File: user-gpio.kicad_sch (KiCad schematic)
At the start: 96 parts, among them J10 62732020621, J11 62703420621, J4 BM04B-SRSS-TB-LF-SN, J5 SSW-106-02-G-D-RA, J6 SSW-106-02-G-D-RA, J7 BM04B-SRSS-TB-LF-SN, J8 BM04B-SRSS-TB-LF-SN, J9 62704020621, Q10 BSS138PW, Q11 BSS138PW, Q12 IRLML6344TRPBF, Q13 BSS138PW, Q14 BSS138PW, Q15 BSS138PW, Q16 BSS138PW, Q8 BSS138PW, Q9 BSS138PW, SW2 CVS-08TB, U45 TPD4E05U06QDQARQ1, U46 TPD4E05U06QDQARQ1

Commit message: Updated schematic page fields
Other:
- company: (none) -> Antmicro Ltd.
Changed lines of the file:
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@@
   (title_block
     (title "K410T devboard")
-    (date "2023-01-04")
+    (date "2023-01-27")
     (rev "0.0.99")
+    (company "Antmicro Ltd.")
   )
   (junction (at 179.07 182.245) (diameter 0) (color 0 0 0 0)

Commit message: Adding JTAG to FMC connector - in progress
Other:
- company: Antmicro Ltd. -> (none)
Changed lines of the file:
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@@
   (title_block
     (title "K410T devboard")
-    (date "2023-01-27")
+    (date "2023-01-04")
     (rev "0.0.99")
-    (company "Antmicro Ltd.")
   )
   (junction (at 179.07 182.245) (diameter 0) (color 0 0 0 0)

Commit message: Updated local libraries
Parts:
- R168, R353, R354, R355, R356, R357, R358, R359, R360: footprint antmicro-footprints:0402-res -> K410T-devboard-footprints:0402-res; symbol antmicroResistors0402:R_100k_0402 -> K410T-devboard:R_100k_0402

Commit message: Bump revision to 1.0.0. Update name on schematic and PCB sheets
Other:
- title: K410T devboard -> Kintex 410T devboard

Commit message: Introduce component standardization
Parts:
- C213, C214, C215, C216, C217: footprint K410T-devboard-footprints:0402-cap -> K410T-devboard-footprints:C_0402_1005Metric; Author (none) -> Antmicro; License (none) -> Apache-2.0
- D18, D19, D20, D21, D22, D23: value KP-1608CGCK -> LED_G_0603_KP-1608CGCK; footprint K410T-devboard-footprints:LED_0603 -> K410T-devboard-footprints:LED_0603_1608Metric_G; symbol K410T-devboard:KP-1608CGCK -> K410T-devboard:LED_G_0603_KP-1608CGCK; Author (none) -> Antmicro; License (none) -> Apache-2.0; Manufacturer KINGBRIGHT -> Kingbright
- D24: value KP-1608EC -> LED_R_0603_KP-1608EC; footprint K410T-devboard-footprints:LED_0603 -> K410T-devboard-footprints:LED_0603_1608Metric_R; symbol K410T-devboard:KP-1608EC -> K410T-devboard:LED_R_0603_KP-1608EC; Author (none) -> Antmicro; License (none) -> Apache-2.0; Manufacturer KINGBRIGHT -> Kingbright
- D25: value KP-1608QBC-D -> LED_B_0603_KP-1608QBC-D; footprint K410T-devboard-footprints:LED_0603 -> K410T-devboard-footprints:LED_0603_1608Metric_B; symbol K410T-devboard:KP-1608QBC-D -> K410T-devboard:LED_B_0603_KP-1608QBC-D; Author (none) -> Antmicro; License (none) -> Apache-2.0; Manufacturer KINGBRIGHT -> Kingbright
- D34, D35, D36, D37: footprint K410T-devboard-footprints:0603-diode -> K410T-devboard-footprints:ESDA25P35-1U1M; Author (none) -> Antmicro; License (none) -> Apache-2.0
- J10: value 62732020621 -> Conn_2x10_P1.27mm_WE_62732020621; symbol K410T-devboard:62732020621 -> K410T-devboard:Conn_2x10_P1.27mm_WE_62732020621; Author (none) -> Antmicro; License (none) -> Apache-2.0; Manufacturer Wurth Electronics Inc. -> Würth Elektronik
- J11: value 62703420621 -> Conn_2x17_P1.27mm_WE_62703420621; symbol K410T-devboard:62703420621 -> K410T-devboard:Conn_2x17_P1.27mm_WE_62703420621; Author (none) -> Antmicro; License (none) -> Apache-2.0; Manufacturer Wurth Electronics Inc. -> Würth Elektronik
- J4, J7, J8, Q10, Q11, Q12, Q13, Q14, Q15, Q16, Q8, Q9: Author (none) -> Antmicro; License (none) -> Apache-2.0
- J5, J6: value SSW-106-02-G-D-RA -> Conn_2x6_P2.54mm_SAMTEC_SSW-106-02-G-D-RA; symbol K410T-devboard:SSW-106-02-G-D-RA -> K410T-devboard:Conn_2x6_P2.54mm_SAMTEC_SSW-106-02-G-D-RA; Author (none) -> Antmicro; License (none) -> Apache-2.0; Manufacturer Samtec Inc. -> Samtec
- J9: value 62704020621 -> Conn_2x20_P1.27mm_WE_62704020621; symbol K410T-devboard:62704020621 -> K410T-devboard:Conn_2x20_P1.27mm_WE_62704020621; Author (none) -> Antmicro; License (none) -> Apache-2.0; Manufacturer Wurth Electronics Inc. -> Würth Elektronik
- R105, R19: footprint K410T-devboard-footprints:0402-res -> K410T-devboard-footprints:R_0402_1005Metric; Author (none) -> Antmicro; Current (none) -> 1A; License (none) -> Apache-2.0; Manufacturer PANASONIC -> Panasonic
- R106, R107, R108, R109, R110, R111, R112, R113, R114, R115, R116, R117, R118, R119, R120, R121, R122, R123, R124, R125, R126, R127, R128, R129, R130, R131, R134, R135, R136, R137, R138, R139, R142, R143, R144, R145, R146, R147: footprint K410T-devboard-footprints:0402-res -> K410T-devboard-footprints:R_0402_1005Metric; Author (none) -> Antmicro; License (none) -> Apache-2.0; Manufacturer BOURNS -> Bourns; Tolerance (none) -> 1%
- R132, R133: footprint K410T-devboard-footprints:EXB18V -> K410T-devboard-footprints:R_Array_4x0201_Panasonic_EXB18V; Author (none) -> Antmicro; License (none) -> Apache-2.0; Val 4x2k2_0201 -> 4x10k_0201
- R140, R141, R148, R149: footprint K410T-devboard-footprints:0402-res -> K410T-devboard-footprints:R_0402_1005Metric; Author (none) -> Antmicro; License (none) -> Apache-2.0; MPN CRCW040210K0FKEDHP -> CR0402-FX-1002GLF; Manufacturer VISHAY -> Bourns; Tolerance (none) -> 1%
- R168, R353, R354, R355, R356, R357, R358, R359, R360: footprint K410T-devboard-footprints:0402-res -> K410T-devboard-footprints:R_0402_1005Metric; Author (none) -> Antmicro; License (none) -> Apache-2.0; MPN CRCW0402100KFKEDHP -> CR0402-FX-1003GLF; Manufacturer VISHAY -> Bourns; Tolerance (none) -> 1%
- S2, S3, S4, S5: value KMR2 -> SW_SPST_KMR211NGLFS; symbol K410T-devboard:KMR2 -> K410T-devboard:SW_SPST_KMR211NGLFS; Author (none) -> Antmicro; License (none) -> Apache-2.0; Manufacturer C&K Components -> C&K
- SW2: value CVS-08TB -> SW_CVS-08TB; symbol K410T-devboard:CVS-08TB -> K410T-devboard:SW_CVS-08TB; Author (none) -> Antmicro; License (none) -> Apache-2.0; Manufacturer Nidec Copal -> Nidec
- U45, U46: footprint K410T-devboard-footprints:USON-10_2.5x1.0mm_P0.5mm -> K410T-devboard-footprints:USON-10_2.5x1mm_P0.5mm; Author (none) -> Antmicro; License (none) -> Apache-2.0
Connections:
- net +3V3: now also C214.2, C215.2; no longer C214.1, C215.1
- net +5V: now also C213.2, C216.2, C217.2; no longer C213.1, C216.1, C217.1
- net GND: now also C213.1, C214.1, C215.1, C216.1, C217.1, D34.1 (K), D35.1 (K), D36.1 (K), D37.1 (K), J4.MP, J7.MP, J8.MP, SW2.17; no longer C213.2, C214.2, C215.2, C216.2, C217.2, D34.2, D35.2, D36.2, D37.2
- net USER_IO.BUTTON0: now also D35.2 (A); no longer D35.1
- net USER_IO.BUTTON1: now also D34.2 (A); no longer D34.1
- net USER_IO.BUTTON2: now also D37.2 (A); no longer D37.1
- net USER_IO.BUTTON3: now also D36.2 (A); no longer D36.1
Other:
- moved on the sheet: C213, C214, C215, C216, C217, R105, R106, R134, R135, R136, R137, R138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

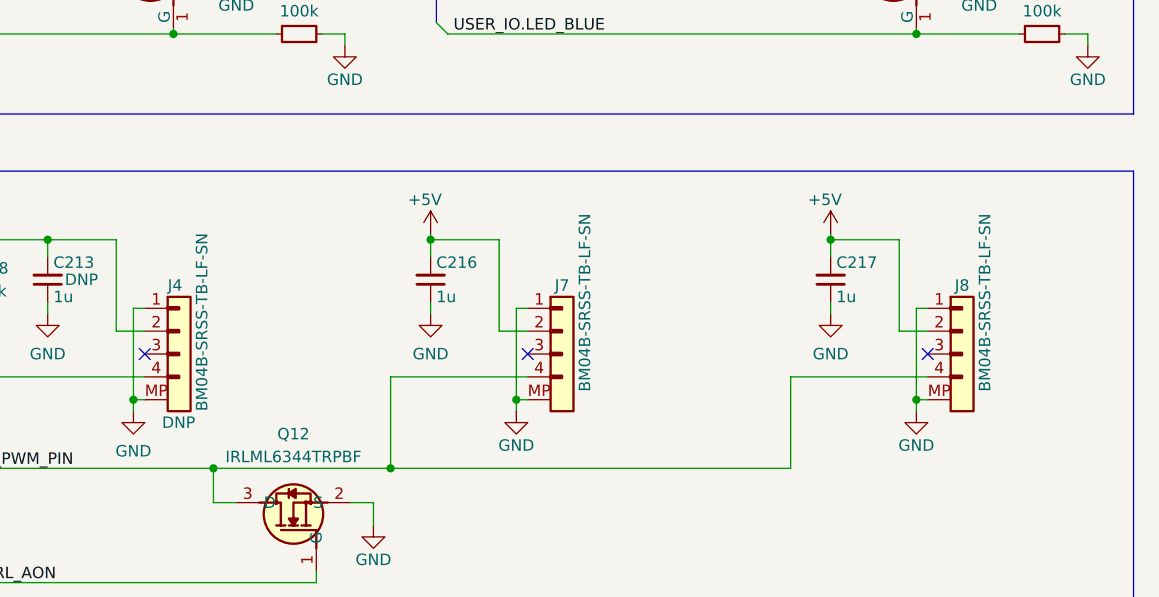
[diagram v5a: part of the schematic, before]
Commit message: [#50532] Update JST connectors footprints
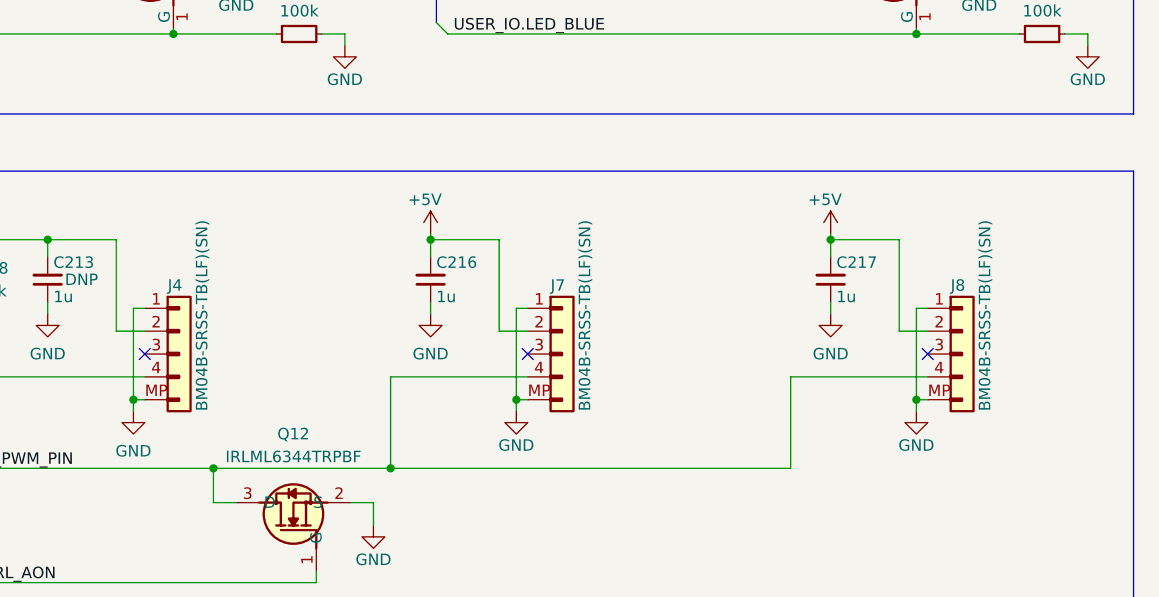
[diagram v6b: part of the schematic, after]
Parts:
- removed J4, J7, J8: BM04B-SRSS-TB-LF-SN, K410T-devboard-footprints:BM04B-SRSS-TB-LF-SN, symbol K410T-devboard:BM04B-SRSS-TB-LF-SN
- added J4, J7, J8: JST_SH_1x4_BM04B-SRSS-TB-LF-SN, K410T-devboard-footprints:Conn_JST_SH_1x4_BM04B-SRSS-TB-LF-SN, symbol K410T-devboard:JST_SH_1x4_BM04B-SRSS-TB-LF-SN
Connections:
- net +5V: now also J4.2 (Pin_2), J7.2 (Pin_2), J8.2 (Pin_2)
- net FAN_PWM_PIN: now also J7.4 (Pin_4), J8.4 (Pin_4)
- net GND: now also J4.1 (Pin_1), J4.MP, J7.1 (Pin_1), J7.MP, J8.1 (Pin_1), J8.MP
- net at R168.1: now also J4.4 (Pin_4)
